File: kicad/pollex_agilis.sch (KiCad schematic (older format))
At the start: 36 parts

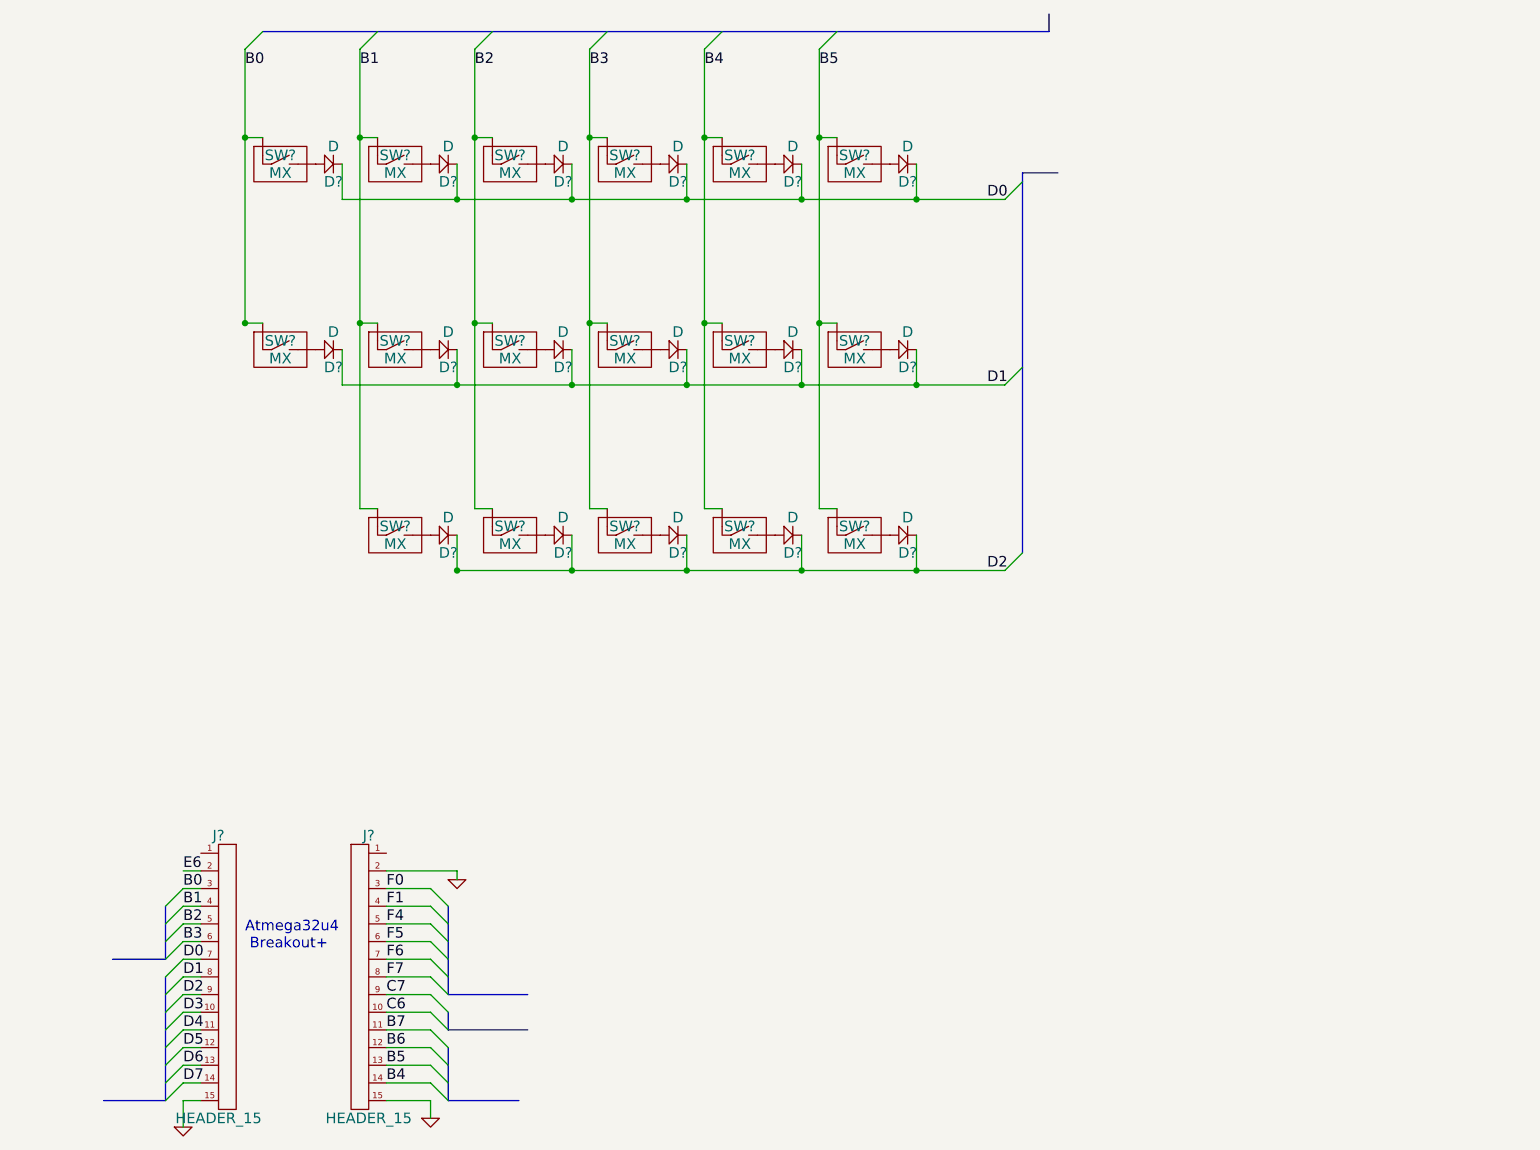
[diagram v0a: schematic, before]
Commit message: first layout + added connectors to thumb and right side board
added footprints for the connectors
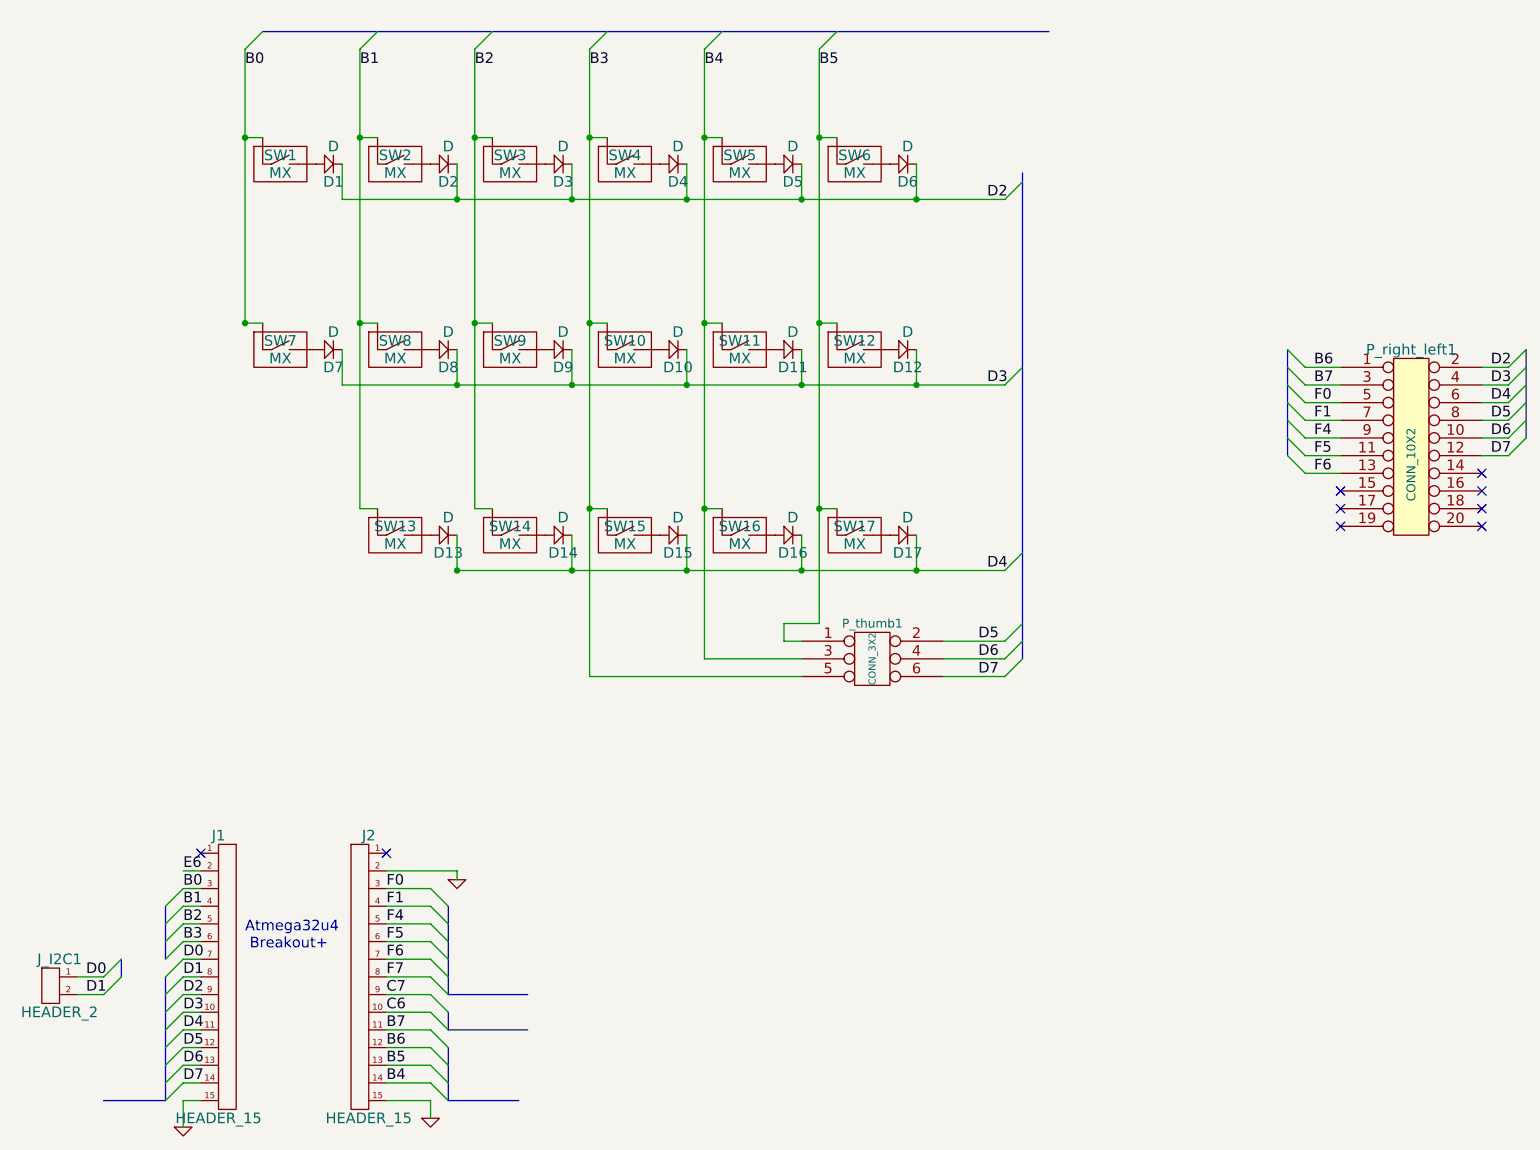
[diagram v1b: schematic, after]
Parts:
- added J_I2C1: HEADER_2, symbol HEADER_2
- added P_right_left1: CONN_10X2, symbol CONN_10X2
- added P_thumb1: CONN_3X2, symbol CONN_3X2
- gave numbers to parts that had none: 36
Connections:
- net B3: now also P_thumb1.5
- net B4: now also P_thumb1.3
- net B5: now also P_thumb1.1
- net B6: now also P_right_left1.1 (P1)
- net B7: now also P_right_left1.3 (P3)
- net D0: now also J_I2C1.1; no longer D1.2 (B), D2.2 (B), D3.2 (B), D4.2 (B), D5.2 (B), D6.2 (B)
- net D1: now also J_I2C1.2; no longer D10.2 (B), D11.2 (B), D12.2 (B), D7.2 (B), D8.2 (B), D9.2 (B)
- net D2: now also D1.2 (B), D2.2 (B), D3.2 (B), D4.2 (B), D5.2 (B), D6.2 (B), P_right_left1.2 (P2); no longer D13.2 (B), D14.2 (B), D15.2 (B), D16.2 (B), D17.2 (B)
- net D3: now also D10.2 (B), D11.2 (B), D12.2 (B), D7.2 (B), D8.2 (B), D9.2 (B), P_right_left1.4 (P4)
- net D4: now also D13.2 (B), D14.2 (B), D15.2 (B), D16.2 (B), D17.2 (B), P_right_left1.6 (P6)
- net D5: now also P_right_left1.8 (P8), P_thumb1.2
- net D6: now also P_right_left1.10 (P10), P_thumb1.4
- net D7: now also P_right_left1.12 (P12), P_thumb1.6
- net F0: now also P_right_left1.5 (P5)
- net F1: now also P_right_left1.7 (P7)
- net F4: now also P_right_left1.9 (P9)
- net F5: now also P_right_left1.11 (P11)
- net F6: now also P_right_left1.13 (P13)
- no-connect marks 0 -> 9
